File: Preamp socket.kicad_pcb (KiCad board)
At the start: 2 copper layers, 23 x 18.6 mm, 7 parts, among them J1 In, J2 VCC, J3 Out, J4 GND, U1 Preamp

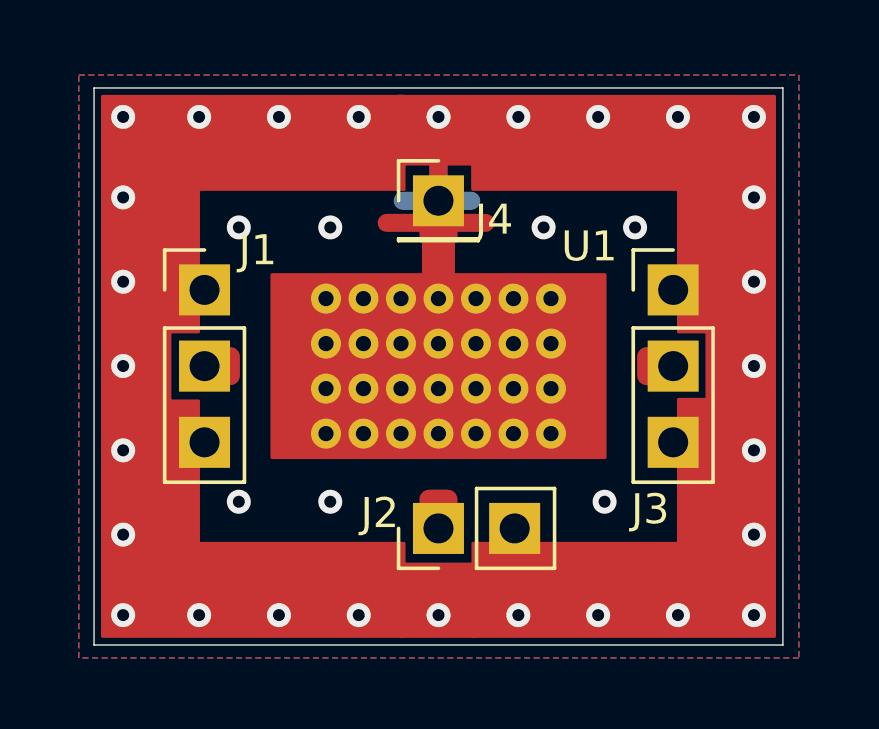
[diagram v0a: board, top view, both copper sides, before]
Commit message: Changed: adjusted for shield clips
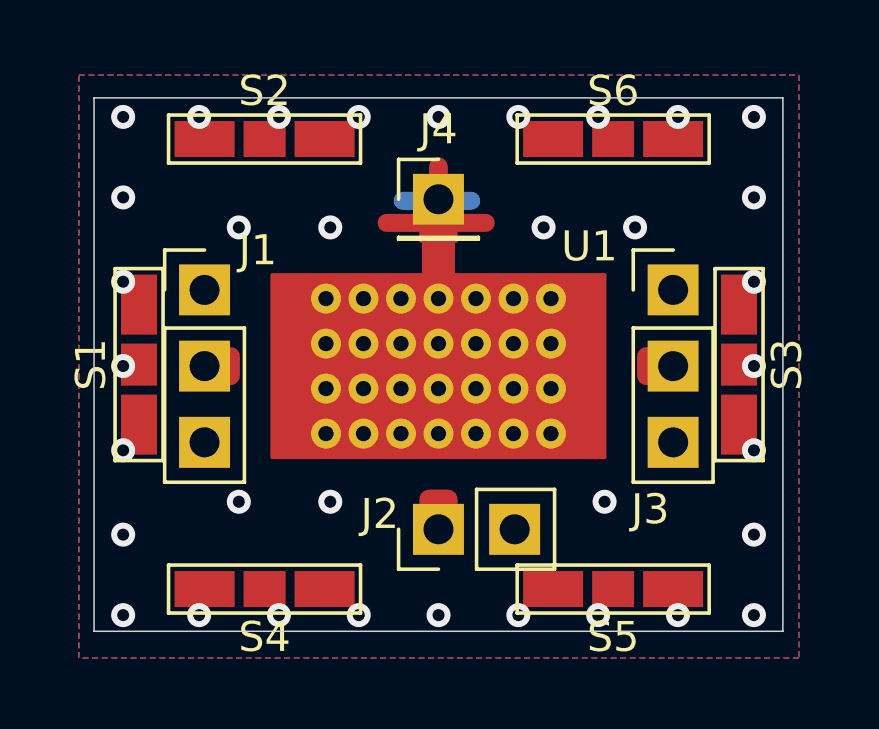
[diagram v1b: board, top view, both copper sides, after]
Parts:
- removed Sh1: RF_Shield_One_Piece, _Custom_footprints:Preamp_shield
- added S1: shield_clip, _Custom:S0971-46R-shield_clip, F.Cu at (147.0, 99.1)
- added S2: shield_clip, _Custom:S0971-46R-shield_clip, F.Cu at (151.2, 91.5)
- added S3: shield_clip, _Custom:S0971-46R-shield_clip, F.Cu at (167.0, 99.1)
- added S4: shield_clip, _Custom:S0971-46R-shield_clip, F.Cu at (151.2, 106.5)
- added S5: shield_clip, _Custom:S0971-46R-shield_clip, F.Cu at (162.8, 106.5)
- added S6: shield_clip, _Custom:S0971-46R-shield_clip, F.Cu at (162.8, 91.5)
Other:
- board size 23 x 18.6 mm -> 23 x 17.8 mm

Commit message: Changed: better outlining of parts
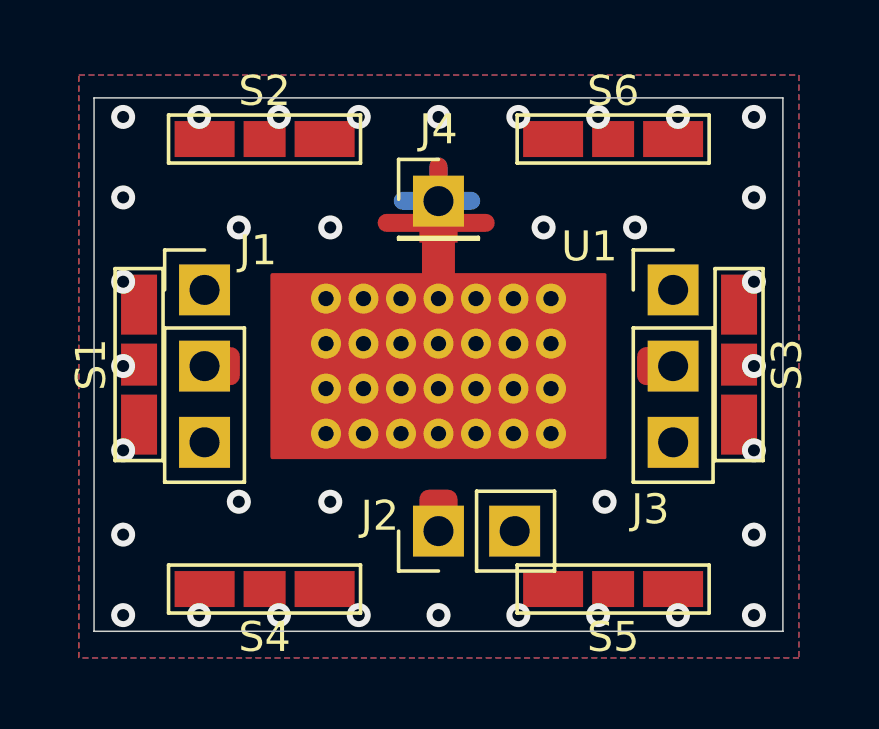
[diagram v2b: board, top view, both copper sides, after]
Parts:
- moved J2 0.06 mm to (157.0, 104.6)
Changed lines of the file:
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@@
     (34 B.Paste user)
     (35 F.Paste user)
-    (36 B.SilkS user hide)
+    (36 B.SilkS user)
     (37 F.SilkS user)
     (38 B.Mask user hide)
@@
     (fp_line (start 1.27 -1.27) (end 1.27 1.27) (layer F.Fab) (width 0.1))
     (fp_line (start -0.635 -1.27) (end 1.27 -1.27) (layer F.Fab) (width 0.1))
-    (pad 1 thru_hole rect (at 0 0) (size 1.7 1.7) (drill 1) (layers *.Cu *.Mask)
+    (pad 1 thru_hole rect (at 0 0.0608) (size 1.7 1.7) (drill 1) (layers *.Cu *.Mask)
       (net 2 GND))
     (model ${KISYS3DMOD}/Connector_PinHeader_2.54mm.3dshapes/PinHeader_1x01_P2.54mm_Vertical.wrl
@@
   )
   (module Connector_PinHeader_2.54mm:PinHeader_1x02_P2.54mm_Vertical (layer F.Cu)
-    (at 157.0228 104.55 90)
+    (at 157.0228 104.6108 90)
     (descr "Through hole straight pin header, 1x02, 2.54mm pitch, single row")
     (tags "Through hole pin header THT 1x02 2.54mm single row")

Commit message: Chnaged: via locations
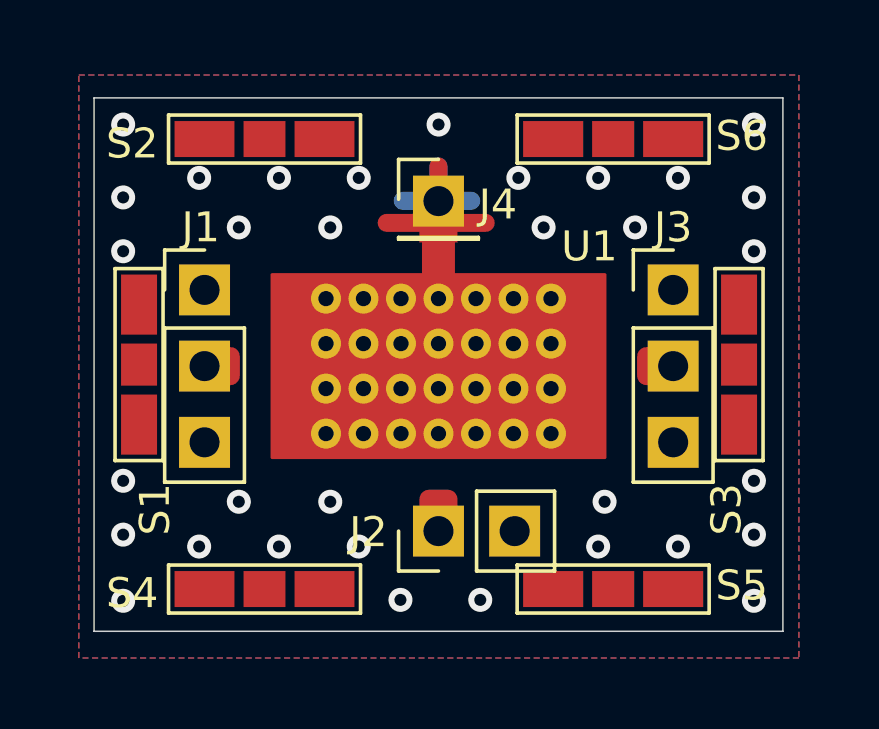
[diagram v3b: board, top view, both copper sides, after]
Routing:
- net GND: vias 35 -> 33
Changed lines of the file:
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@@
     (thickness 1.6)
     (drawings 11)
-    (tracks 40)
+    (tracks 38)
     (zones 0)
     (modules 12)
@@
     (solder_mask_min_width 0.25)
     (aux_axis_origin 0 0)
-    (visible_elements 7FF3FF77)
+    (visible_elements 7FF7FF7F)
     (pcbplotparams
       (layerselection 0x010fc_ffffffff)
@@
     (add_net "Net-(J3-Pad2)")
   )
-  (module Connector_PinHeader_2.54mm:PinHeader_1x01_P2.54mm_Vertical (layer F.Cu)
+  (module Connector_PinHeader_2.54mm:PinHeader_1x01_P2.54mm_Vertical locked (layer F.Cu)
     (at 157.0228 93.55)
     (descr "Through hole straight pin header, 1x01, 2.54mm pitch, single row")
     (tags "Through hole pin header THT 1x01 2.54mm single row")
-    (fp_text reference J4 (at 0 -2.33) (layer F.SilkS)
+    (fp_text reference J4 (at 1.9812 0.176) (layer F.SilkS)
       (effects (font (size 1 1) (thickness 0.15)))
     )
@@
       (net 2 GND))
     (model ${KISYS3DMOD}/Connector_PinHeader_2.54mm.3dshapes/PinHeader_1x01_P2.54mm_Vertical.wrl
-      (at (xyz 0 0 0))
+      (offset (xyz 0 0 -1.6))
       (scale (xyz 1 1 1))
-      (rotate (xyz 0 0 0))
-    )
-  )
-  (module Connector_PinHeader_2.54mm:PinHeader_1x02_P2.54mm_Vertical (layer F.Cu)
+      (rotate (xyz 0 180 0))
+    )
+  )
+  (module Connector_PinHeader_2.54mm:PinHeader_1x02_P2.54mm_Vertical locked (layer F.Cu)
     (at 157.0228 104.6108 90)
     (descr "Through hole straight pin header, 1x02, 2.54mm pitch, single row")
     (tags "Through hole pin header THT 1x02 2.54mm single row")
-    (fp_text reference J2 (at 0.508 -1.9558 180) (layer F.SilkS)
+    (fp_text reference J2 (at -0.0372 -2.3368 180) (layer F.SilkS)
       (effects (font (size 1 1) (thickness 0.15)))
     )
@@
       (net 1 "Net-(J2-Pad1)"))
     (model ${KISYS3DMOD}/Connector_PinHeader_2.54mm.3dshapes/PinHeader_1x02_P2.54mm_Vertical.wrl
-      (at (xyz 0 0 0))
+      (offset (xyz 0 0 -1.6))
       (scale (xyz 1 1 1))
-      (rotate (xyz 0 0 0))
+      (rotate (xyz 0 180 0))
     )
   )
@@
     (descr "Through hole straight pin header, 1x03, 2.54mm pitch, single row")
     (tags "Through hole pin header THT 1x03 2.54mm single row")
-    (fp_text reference J3 (at -0.762 7.3152) (layer F.SilkS)
+    (fp_text reference J3 (at 0 -2.0828) (layer F.SilkS)
       (effects (font (size 1 1) (thickness 0.15)))
     )
@@
       (net 2 GND))
     (model ${KISYS3DMOD}/Connector_PinHeader_2.54mm.3dshapes/PinHeader_1x03_P2.54mm_Vertical.wrl
-      (at (xyz 0 0 0))
+      (offset (xyz 0 0 -1.6))
       (scale (xyz 1 1 1))
-      (rotate (xyz 0 0 0))
+      (rotate (xyz 0 180 0))
     )
   )
@@
     (descr "Through hole straight pin header, 1x03, 2.54mm pitch, single row")
     (tags "Through hole pin header THT 1x03 2.54mm single row")
-    (fp_text reference J1 (at 1.778 -1.3208) (layer F.SilkS)
+    (fp_text reference J1 (at -0.127 -2.0828) (layer F.SilkS)
       (effects (font (size 1 1) (thickness 0.15)))
     )
@@
       (net 2 GND))
     (model ${KISYS3DMOD}/Connector_PinHeader_2.54mm.3dshapes/PinHeader_1x03_P2.54mm_Vertical.wrl
-      (at (xyz 0 0 0))
+      (offset (xyz 0 0 -1.6))
       (scale (xyz 1 1 1))
-      (rotate (xyz 0 0 0))
+      (rotate (xyz 0 180 0))
     )
   )
   (module _Custom:S0971-46R-shield_clip (layer F.Cu)
     (at 162.846 91.542)
-    (fp_text reference S6 (at 0 -1.6) (layer F.SilkS)
+    (fp_text reference S6 (at 4.286 -0.102) (layer F.SilkS)
       (effects (font (size 1 1) (thickness 0.15)))
     )
@@
   (module _Custom:S0971-46R-shield_clip (layer F.Cu)
     (at 162.846 106.542 180)
-    (fp_text reference S5 (at 0 -1.6) (layer F.SilkS)
+    (fp_text reference S5 (at -4.286 0.116) (layer F.SilkS)
       (effects (font (size 1 1) (thickness 0.15)))
     )
@@
   (module _Custom:S0971-46R-shield_clip (layer F.Cu)
     (at 151.225 106.542 180)
-    (fp_text reference S4 (at 0 -1.6) (layer F.SilkS)
+    (fp_text reference S4 (at 4.413 -0.138) (layer F.SilkS)
       (effects (font (size 1 1) (thickness 0.15)))
     )
@@
   (module _Custom:S0971-46R-shield_clip (layer F.Cu)
     (at 167.042 99.06 270)
-    (fp_text reference S3 (at 0 -1.6 90) (layer F.SilkS)
+    (fp_text reference S3 (at 4.826 0.418 90) (layer F.SilkS)
       (effects (font (size 1 1) (thickness 0.15)))
     )
@@
   (module _Custom:S0971-46R-shield_clip (layer F.Cu)
     (at 151.225 91.542)
-    (fp_text reference S2 (at 0 -1.6) (layer F.SilkS)
+    (fp_text reference S2 (at -4.413 0.152) (layer F.SilkS)
       (effects (font (size 1 1) (thickness 0.15)))
     )
@@
   (module _Custom:S0971-46R-shield_clip (layer F.Cu)
     (at 147.042 99.06 90)
-    (fp_text reference S1 (at 0 -1.6 90) (layer F.SilkS)
+    (fp_text reference S1 (at -4.826 0.532 90) (layer F.SilkS)
       (effects (font (size 1 1) (thickness 0.15)))
     )
@@
   (gr_line (start 168.5036 107.95) (end 145.542 107.95) (layer Edge.Cuts) (width 0.05))
   (gr_line (start 168.5036 90.17) (end 168.5036 107.95) (layer Edge.Cuts) (width 0.05))
-  (via (at 167.5384 90.805) (size 0.8) (drill 0.4) (layers F.Cu B.Cu) (net 2))
+  (via (at 167.5384 91.059) (size 0.8) (drill 0.4) (layers F.Cu B.Cu) (net 2))
   (segment (start 155.2956 94.3356) (end 158.5976 94.3356) (width 0.6) (layer F.Cu) (net 2))
   (segment (start 157.0228 94.3558) (end 157.0228 96.8608) (width 0.25) (layer F.Cu) (net 2))
-  (via (at 165.0054 90.805) (size 0.8) (drill 0.4) (layers F.Cu B.Cu) (net 2))
-  (via (at 162.3454 90.805) (size 0.8) (drill 0.4) (layers F.Cu B.Cu) (net 2))
-  (via (at 159.6854 90.805) (size 0.8) (drill 0.4) (layers F.Cu B.Cu) (net 2))
-  (via (at 157.0254 90.805) (size 0.8) (drill 0.4) (layers F.Cu B.Cu) (net 2))
-  (via (at 154.3654 90.805) (size 0.8) (drill 0.4) (layers F.Cu B.Cu) (net 2))
-  (via (at 151.7054 90.805) (size 0.8) (drill 0.4) (layers F.Cu B.Cu) (net 2))
-  (via (at 149.0454 90.805) (size 0.8) (drill 0.4) (layers F.Cu B.Cu) (net 2))
-  (via (at 146.5124 90.805) (size 0.8) (drill 0.4) (layers F.Cu B.Cu) (net 2))
+  (via (at 165.0054 92.837) (size 0.8) (drill 0.4) (layers F.Cu B.Cu) (net 2))
+  (via (at 159.6854 92.837) (size 0.8) (drill 0.4) (layers F.Cu B.Cu) (net 2))
+  (via (at 157.0254 91.059) (size 0.8) (drill 0.4) (layers F.Cu B.Cu) (net 2))
+  (via (at 154.3654 92.837) (size 0.8) (drill 0.4) (layers F.Cu B.Cu) (net 2))
+  (via (at 149.0454 92.837) (size 0.8) (drill 0.4) (layers F.Cu B.Cu) (net 2))
+  (via (at 146.5124 91.059) (size 0.8) (drill 0.4) (layers F.Cu B.Cu) (net 2))
   (via (at 167.5384 93.488) (size 0.8) (drill 0.4) (layers F.Cu B.Cu) (net 2))
-  (via (at 167.5384 96.298) (size 0.8) (drill 0.4) (layers F.Cu B.Cu) (net 2))
-  (via (at 167.5384 99.108) (size 0.8) (drill 0.4) (layers F.Cu B.Cu) (net 2))
-  (via (at 167.5384 101.918) (size 0.8) (drill 0.4) (layers F.Cu B.Cu) (net 2))
+  (via (at 167.5384 95.282) (size 0.8) (drill 0.4) (layers F.Cu B.Cu) (net 2))
+  (via (at 167.5384 102.934) (size 0.8) (drill 0.4) (layers F.Cu B.Cu) (net 2))
   (via (at 167.5384 104.728) (size 0.8) (drill 0.4) (layers F.Cu B.Cu) (net 2))
-  (via (at 167.5384 107.411) (size 0.8) (drill 0.4) (layers F.Cu B.Cu) (net 2))
+  (via (at 167.5384 106.934) (size 0.8) (drill 0.4) (layers F.Cu B.Cu) (net 2))
   (via (at 146.5124 93.488) (size 0.8) (drill 0.4) (layers F.Cu B.Cu) (net 2))
-  (via (at 146.5124 96.298) (size 0.8) (drill 0.4) (layers F.Cu B.Cu) (net 2))
-  (via (at 146.5124 99.108) (size 0.8) (drill 0.4) (layers F.Cu B.Cu) (net 2))
-  (via (at 146.5124 101.918) (size 0.8) (drill 0.4) (layers F.Cu B.Cu) (net 2))
+  (via (at 146.5124 95.282) (size 0.8) (drill 0.4) (layers F.Cu B.Cu) (net 2))
+  (via (at 146.5124 102.934) (size 0.8) (drill 0.4) (layers F.Cu B.Cu) (net 2))
   (via (at 146.5124 104.728) (size 0.8) (drill 0.4) (layers F.Cu B.Cu) (net 2))
-  (via (at 165.0054 107.411) (size 0.8) (drill 0.4) (layers F.Cu B.Cu) (net 2))
-  (via (at 162.3454 107.411) (size 0.8) (drill 0.4) (layers F.Cu B.Cu) (net 2))
-  (via (at 159.6854 107.411) (size 0.8) (drill 0.4) (layers F.Cu B.Cu) (net 2))
-  (via (at 157.0254 107.411) (size 0.8) (drill 0.4) (layers F.Cu B.Cu) (net 2))
-  (via (at 154.3654 107.411) (size 0.8) (drill 0.4) (layers F.Cu B.Cu) (net 2))
-  (via (at 151.7054 107.411) (size 0.8) (drill 0.4) (layers F.Cu B.Cu) (net 2))
-  (via (at 149.0454 107.411) (size 0.8) (drill 0.4) (layers F.Cu B.Cu) (net 2))
-  (via (at 146.5124 107.411) (size 0.8) (drill 0.4) (layers F.Cu B.Cu) (net 2))
+  (via (at 165.0054 105.125) (size 0.8) (drill 0.4) (layers F.Cu B.Cu) (net 2))
+  (via (at 162.3454 105.125) (size 0.8) (drill 0.4) (layers F.Cu B.Cu) (net 2))
+  (via (at 158.4154 106.903) (size 0.8) (drill 0.4) (layers F.Cu B.Cu) (net 2))
+  (via (at 155.7554 106.903) (size 0.8) (drill 0.4) (layers F.Cu B.Cu) (net 2))
+  (via (at 154.3654 105.125) (size 0.8) (drill 0.4) (layers F.Cu B.Cu) (net 2))
+  (via (at 151.7054 105.125) (size 0.8) (drill 0.4) (layers F.Cu B.Cu) (net 2))
+  (via (at 149.0454 105.125) (size 0.8) (drill 0.4) (layers F.Cu B.Cu) (net 2))
+  (via (at 146.5124 106.934) (size 0.8) (drill 0.4) (layers F.Cu B.Cu) (net 2))
   (via (at 150.368 94.488) (size 0.8) (drill 0.4) (layers F.Cu B.Cu) (net 2))
   (via (at 153.416 94.488) (size 0.8) (drill 0.4) (layers F.Cu B.Cu) (net 2))
@@
   (segment (start 155.829 93.599) (end 158.115 93.599) (width 0.6) (layer B.Cu) (net 2))
   (segment (start 157.0228 93.599) (end 157.0228 92.456) (width 0.6) (layer F.Cu) (net 2))
+  (via (at 162.3454 92.837) (size 0.8) (drill 0.4) (layers F.Cu B.Cu) (net 2))
+  (via (at 151.7054 92.837) (size 0.8) (drill 0.4) (layers F.Cu B.Cu) (net 2))
   (zone (net 2) (net_name GND) (layer F.Cu) (hatch edge 0.508)
     (connect_pads (clearance 0))
